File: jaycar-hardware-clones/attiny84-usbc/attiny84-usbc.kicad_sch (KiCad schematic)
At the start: 20 parts, among them J2 Conn_01x03_Socket, J3 USB_C_Receptacle_USB2.0, J4 Conn_01x07_Socket, J5 Conn_01x07_Socket, U1 ATtiny84-20SS, U2 L78L05_SOT89

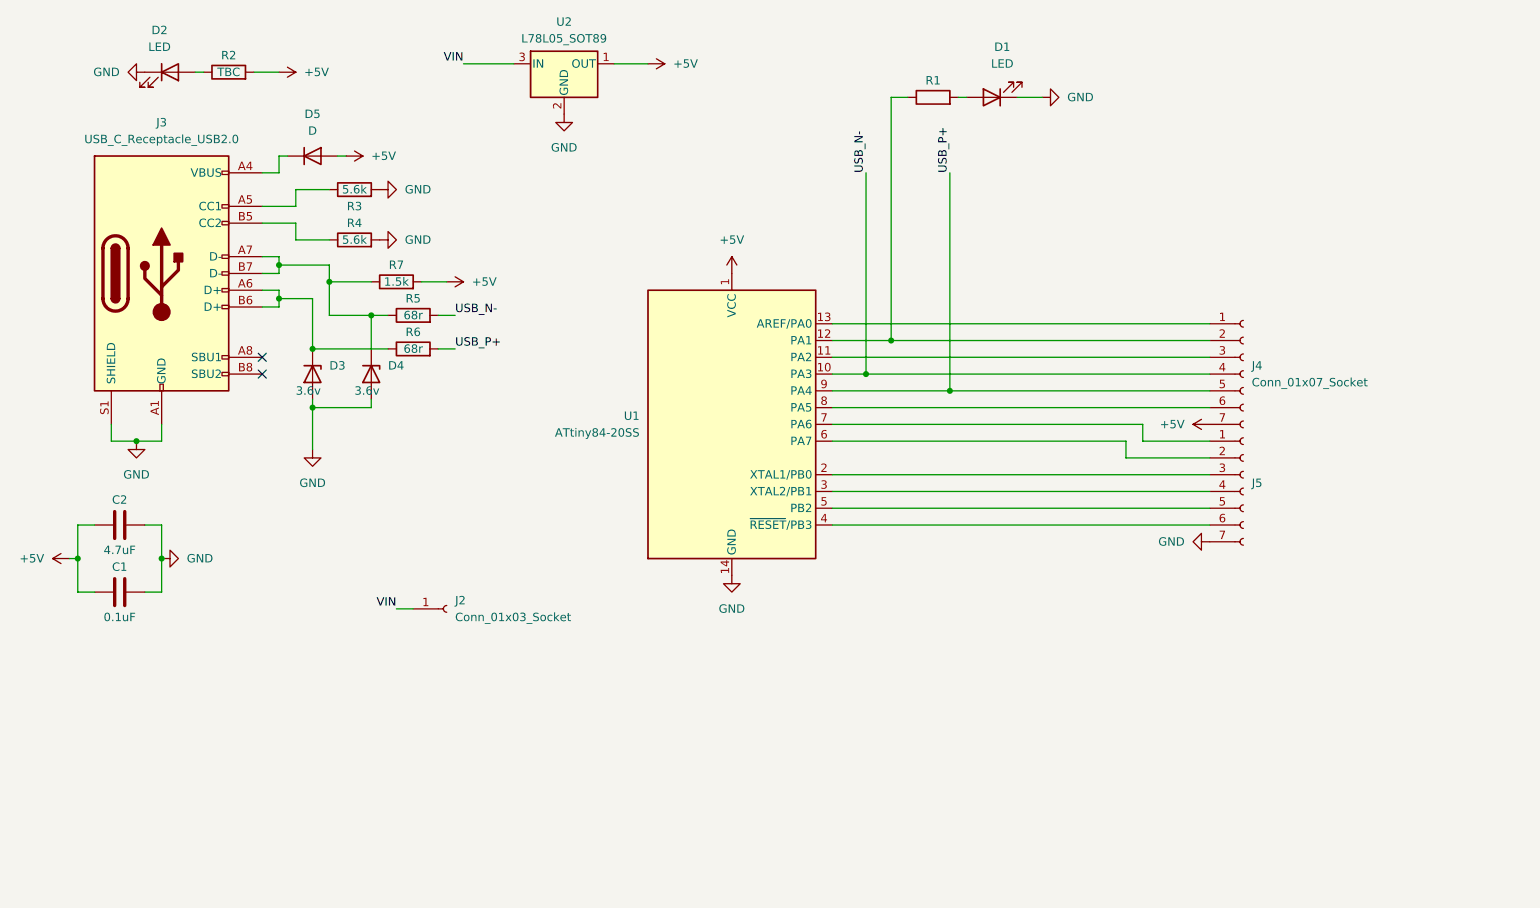
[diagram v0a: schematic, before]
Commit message: changes to attiny84-usbc
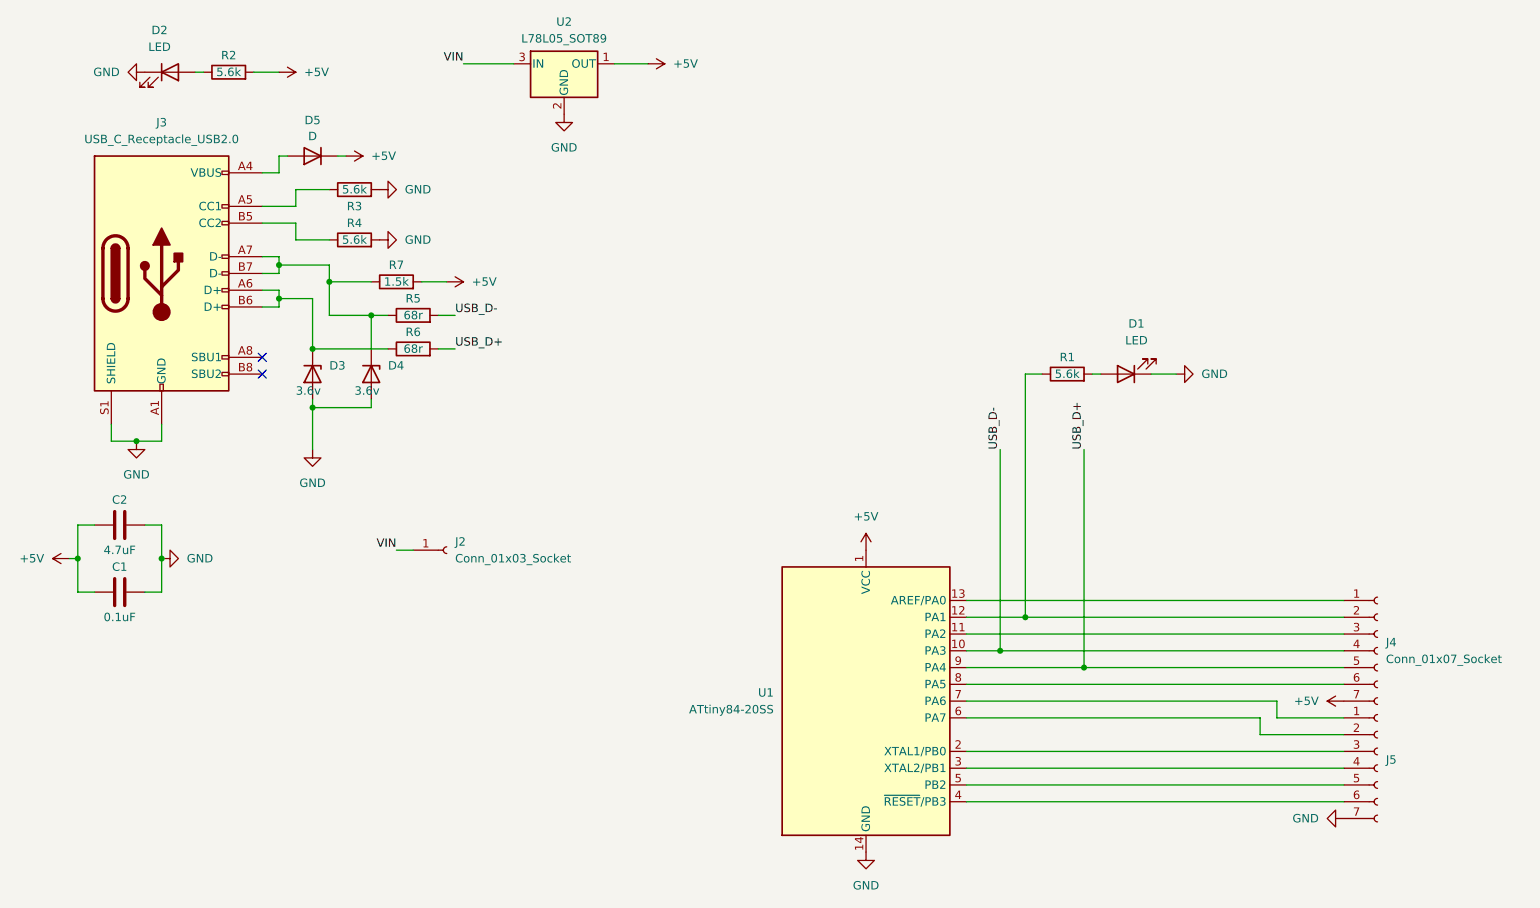
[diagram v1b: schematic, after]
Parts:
- R1, R2: value TBC -> 5.6k
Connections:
- net +5V: now also D5.1 (K); no longer D5.2 (A)
- net at J3.A4 (VBUS), J3.A9 (VBUS), J3.B4 (VBUS)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: now also D5.2 (A); no longer D5.1 (K)
- net USB_N- renamed USB_D-
- net USB_P+ renamed USB_D+
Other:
- moved on the sheet: D1, D5, J2, J4, J5, R1, U1

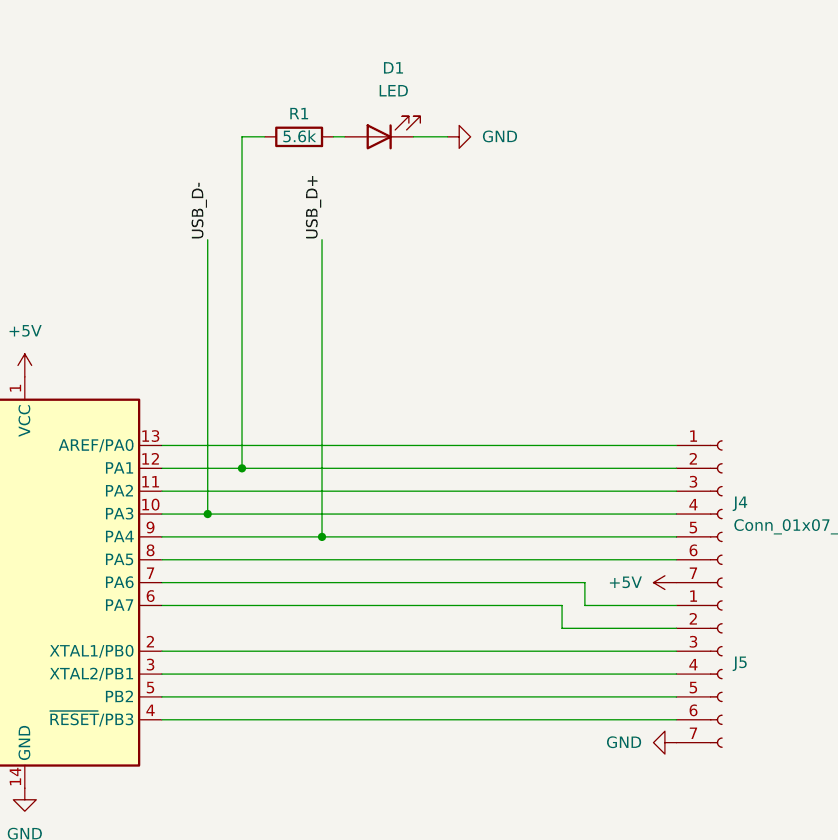
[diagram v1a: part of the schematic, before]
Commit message: new revision of attiny84-c, featuring correct footprints and a slightly better layout
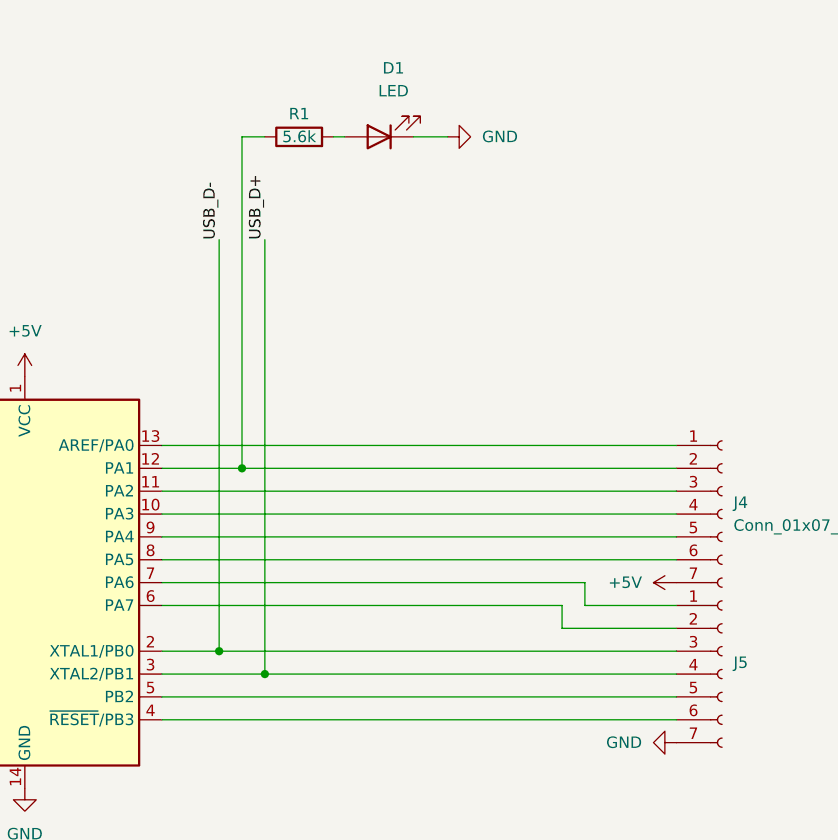
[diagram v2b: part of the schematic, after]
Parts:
- D1, D2: footprint Diode_SMD:D_0805_2012Metric -> Diode_SMD:D_0603_1608Metric
- D3, D4: footprint Diode_SMD:D_0805_2012Metric -> Diode_SMD:D_MiniMELF
- R1: footprint Resistor_SMD:R_0603_1608Metric -> Resistor_SMD:R_0402_1005Metric
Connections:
- net USB_D+: now also J5.4 (Pin_4), U1.3 (XTAL2/PB1); no longer J4.5 (Pin_5), U1.9 (PA4)
- net USB_D-: now also J5.3 (Pin_3), U1.2 (XTAL1/PB0); no longer J4.4 (Pin_4), U1.10 (PA3)
- new net: J4.4 (Pin_4), U1.10 (PA3)
- new net: J4.5 (Pin_5), U1.9 (PA4)
